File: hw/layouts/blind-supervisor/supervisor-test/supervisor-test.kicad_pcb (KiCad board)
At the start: 2 copper layers, 14 parts

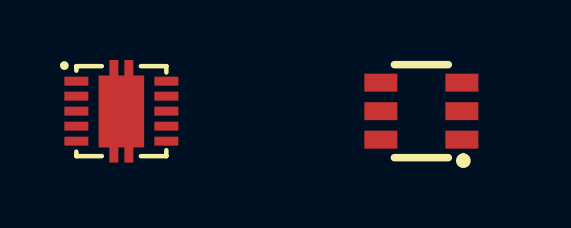
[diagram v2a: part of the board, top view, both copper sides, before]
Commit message: Make the cleaner controller reproducible from circuit source (#3)
* Rebuild cleaner controller from circuit source and verify native previews

* Use compiler-compatible Python without changing native render runtime
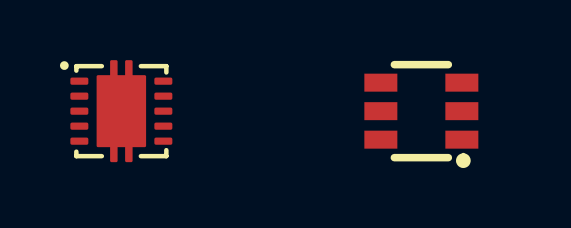
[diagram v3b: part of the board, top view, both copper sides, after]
